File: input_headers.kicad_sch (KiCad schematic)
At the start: 13 parts, among them J1 171857-0003, J2 171856-0002, J6 171856-0002, J7 Conn_01x07, J8 USB_B_Micro, J9 TLW-104-05-T-D, U3 FT230XS-R

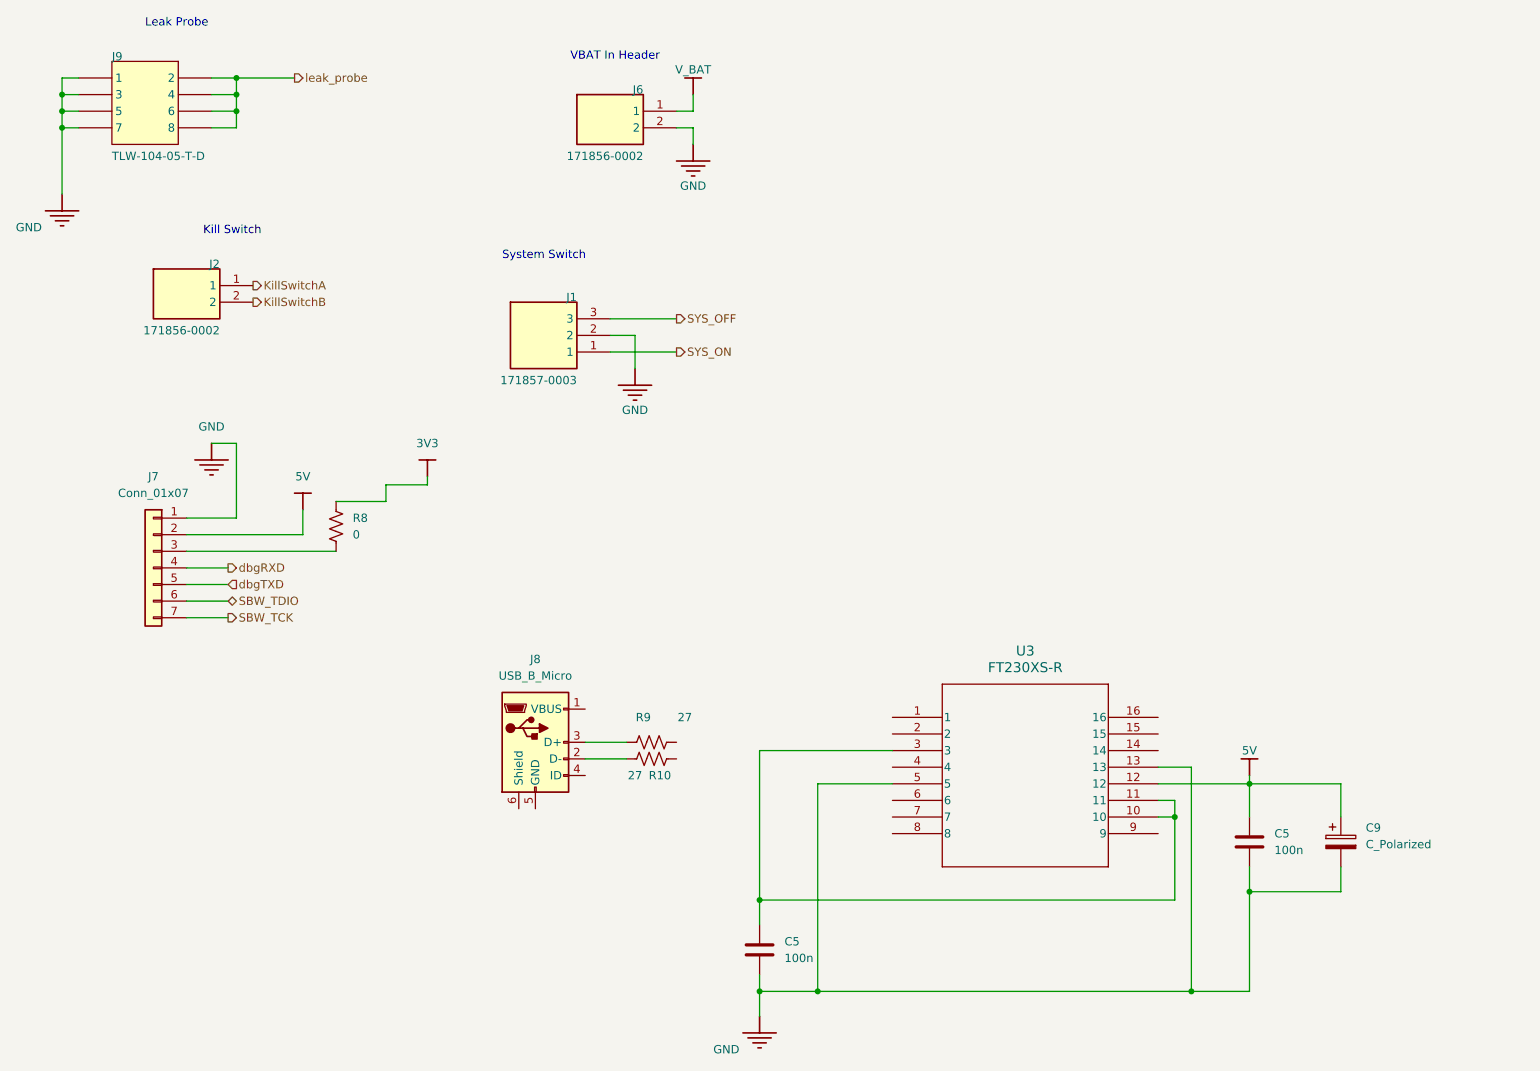
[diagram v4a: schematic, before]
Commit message: updated input headers schematic for FT232 chip
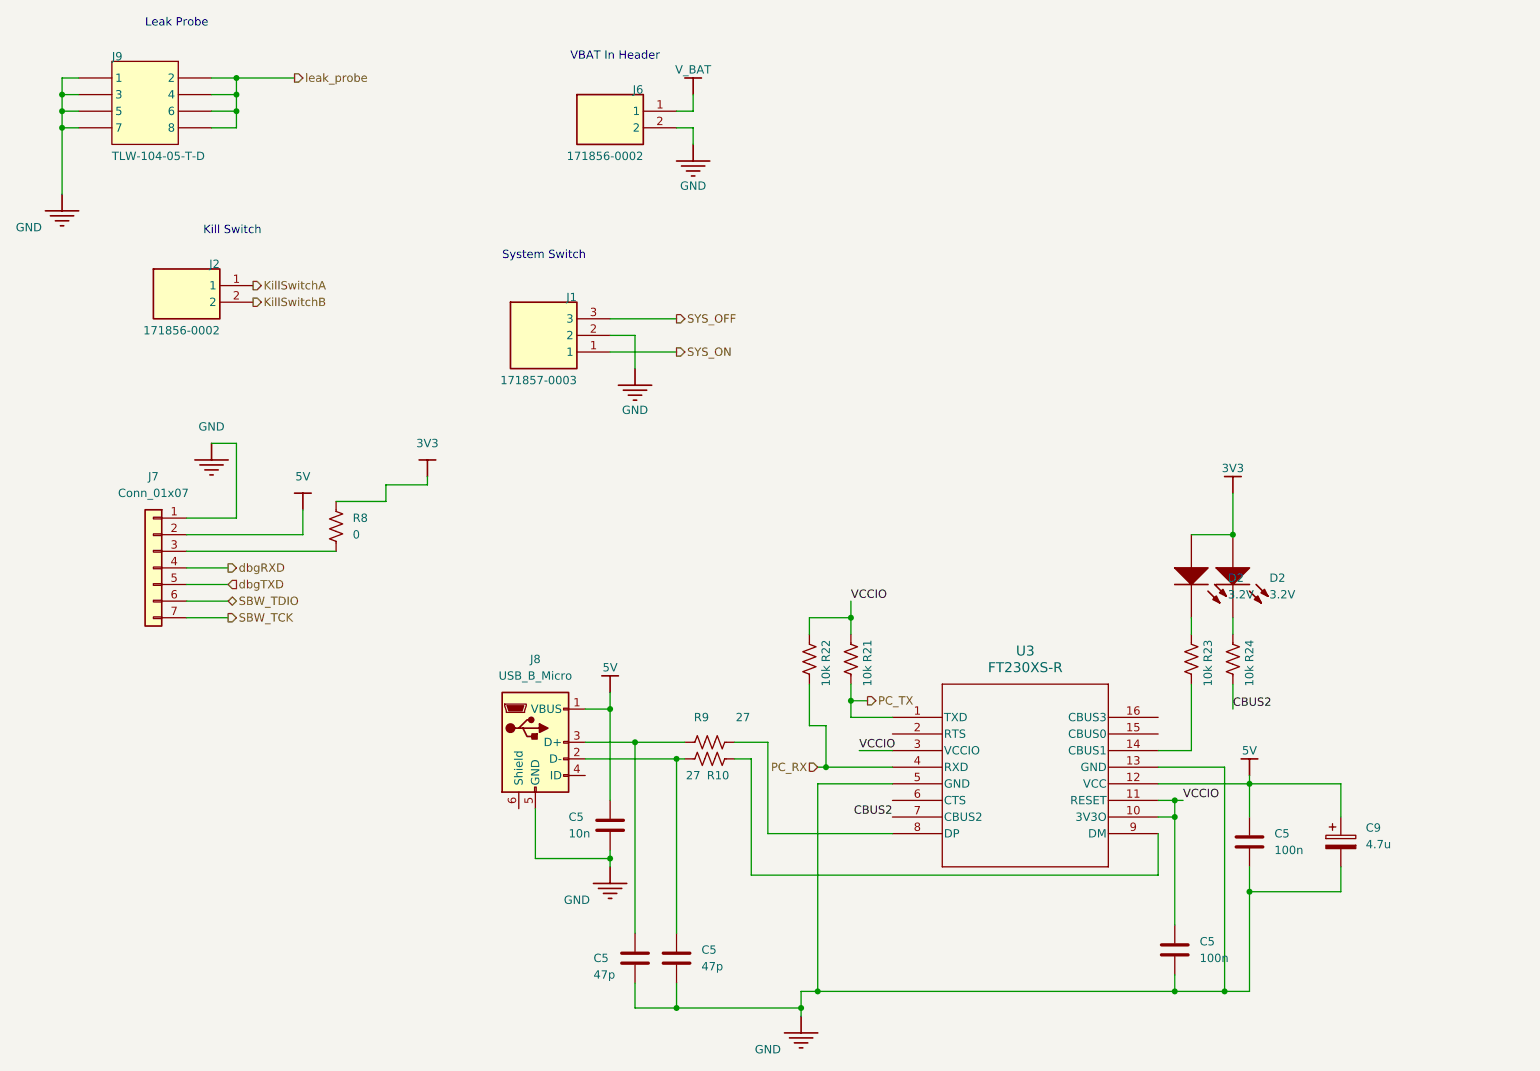
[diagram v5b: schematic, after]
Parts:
- removed C5: 100n, symbol Device:C
- added C5: 10n, symbol Device:C
- added C5 (x2): 47p, symbol Device:C
- added C5: 100n, symbol Device:C
- added D2 (x2): 3.2V, AltiumImport:0805_A, symbol MEB-altium-import:root_3_WE-LED_K1A2-2
- added R21, R22, R23, R24: 10k, symbol Device:R_US
- C9: value C_Polarized -> 4.7u
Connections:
- net 3V3: now also D2.2 (A), D2.2 (A)
- net 5V: now also J8.1 (VBUS), C5.1
- net GND: now also J8.5 (GND), C5.2, C5.2, C5.2, C5.2
- net PC_TX: now reaches U3.1 (TXD)
- net PC_TX: now also R21.1
- net VCCIO: now reaches U3.10 (3V3O), U3.11 (RESET), U3.3 (VCCIO)
- net VCCIO: now also C5.1, R21.2, R22.2
- net at U3.14 (CBUS1): now also R23.1
- net PC_RX: now reaches U3.4 (RXD)
- net PC_RX: now also R22.1
- net CBUS2: now reaches U3.7 (CBUS2)
- net CBUS2: now also R24.1
- net at U3.8 (DP): now also R9.2
- net at U3.9 (DM): now also R10.2
- net at J8.3 (D+), R9.1: now also C5.1
- net at J8.2 (D-), R10.1: now also C5.1
- new net: D2.1 (K), R23.2
- new net: D2.1 (K), R24.2
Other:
- moved on the sheet: R10, R9

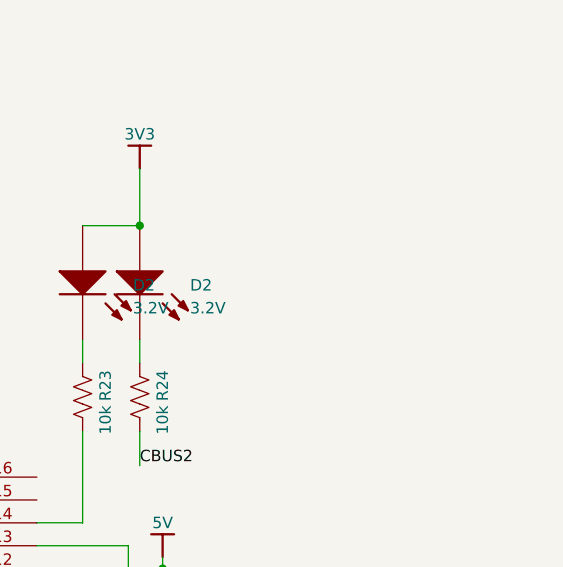
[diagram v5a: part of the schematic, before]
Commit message: Finalized schematic and began assigning footprints
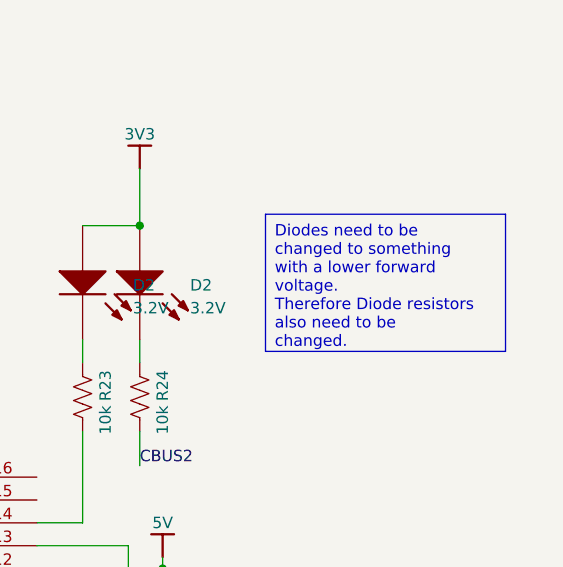
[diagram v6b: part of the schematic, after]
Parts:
- J8: footprint (none) -> Connector_USB:USB_Micro-B_GCT_USB3076-30-A
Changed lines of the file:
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@@
     (stroke (width 0) (type default))
+  )
+  (text_box "Diodes need to be changed to something with a lower forward voltage.\nTherefore Diode resistors also need to be changed.\n"
+    (at 204.47 96.52 0) (size 26.67 15.24)
+    (stroke (width 0) (type default))
+    (fill (type none))
+    (effects (font (size 1.27 1.27)) (justify left top))
   )
   (text "VBAT In Header" (at 102.87 25.4 0)
@@
       (effects (font (size 1.27 1.27)))
     )
-    (property "Footprint" "" (at 87.63 130.81 0)
-      (effects (font (size 1.27 1.27)) hide)
-    )
+    (property "Footprint" "Connector_USB:USB_Micro-B_GCT_USB3076-30-A" (at 87.63 130.81 0)
+      (effects (font (size 1.27 1.27)) hide)
+    )

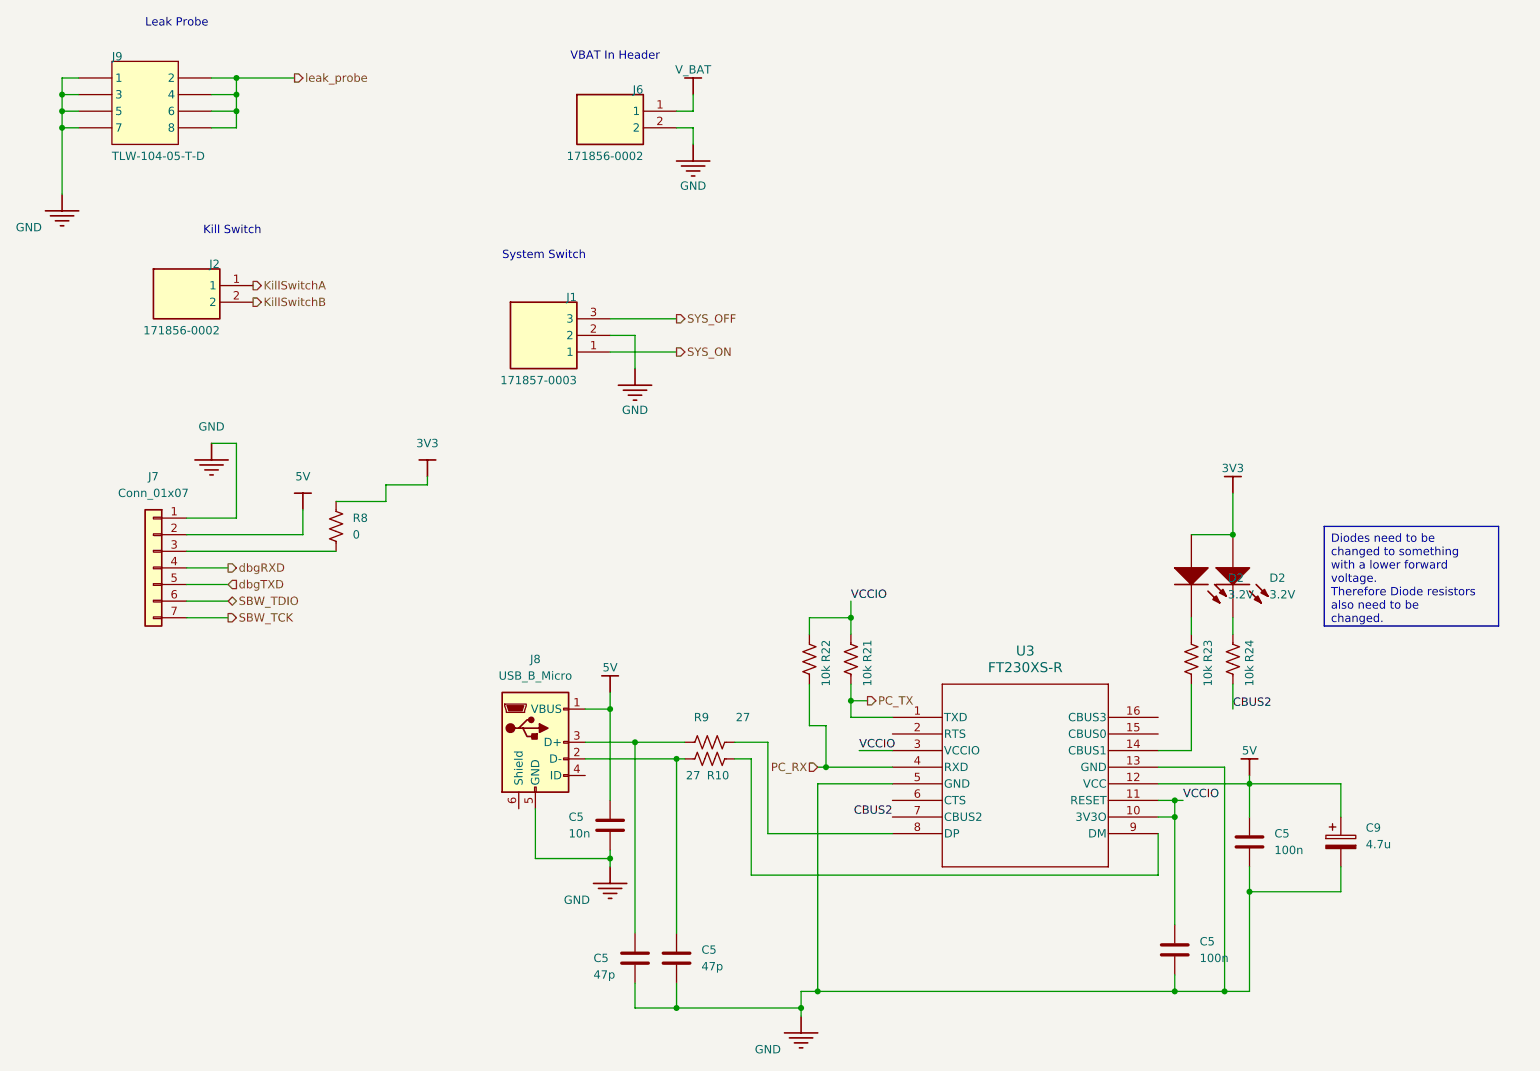
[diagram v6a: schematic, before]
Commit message: updated power and ground symbols in schematic to kicad library version
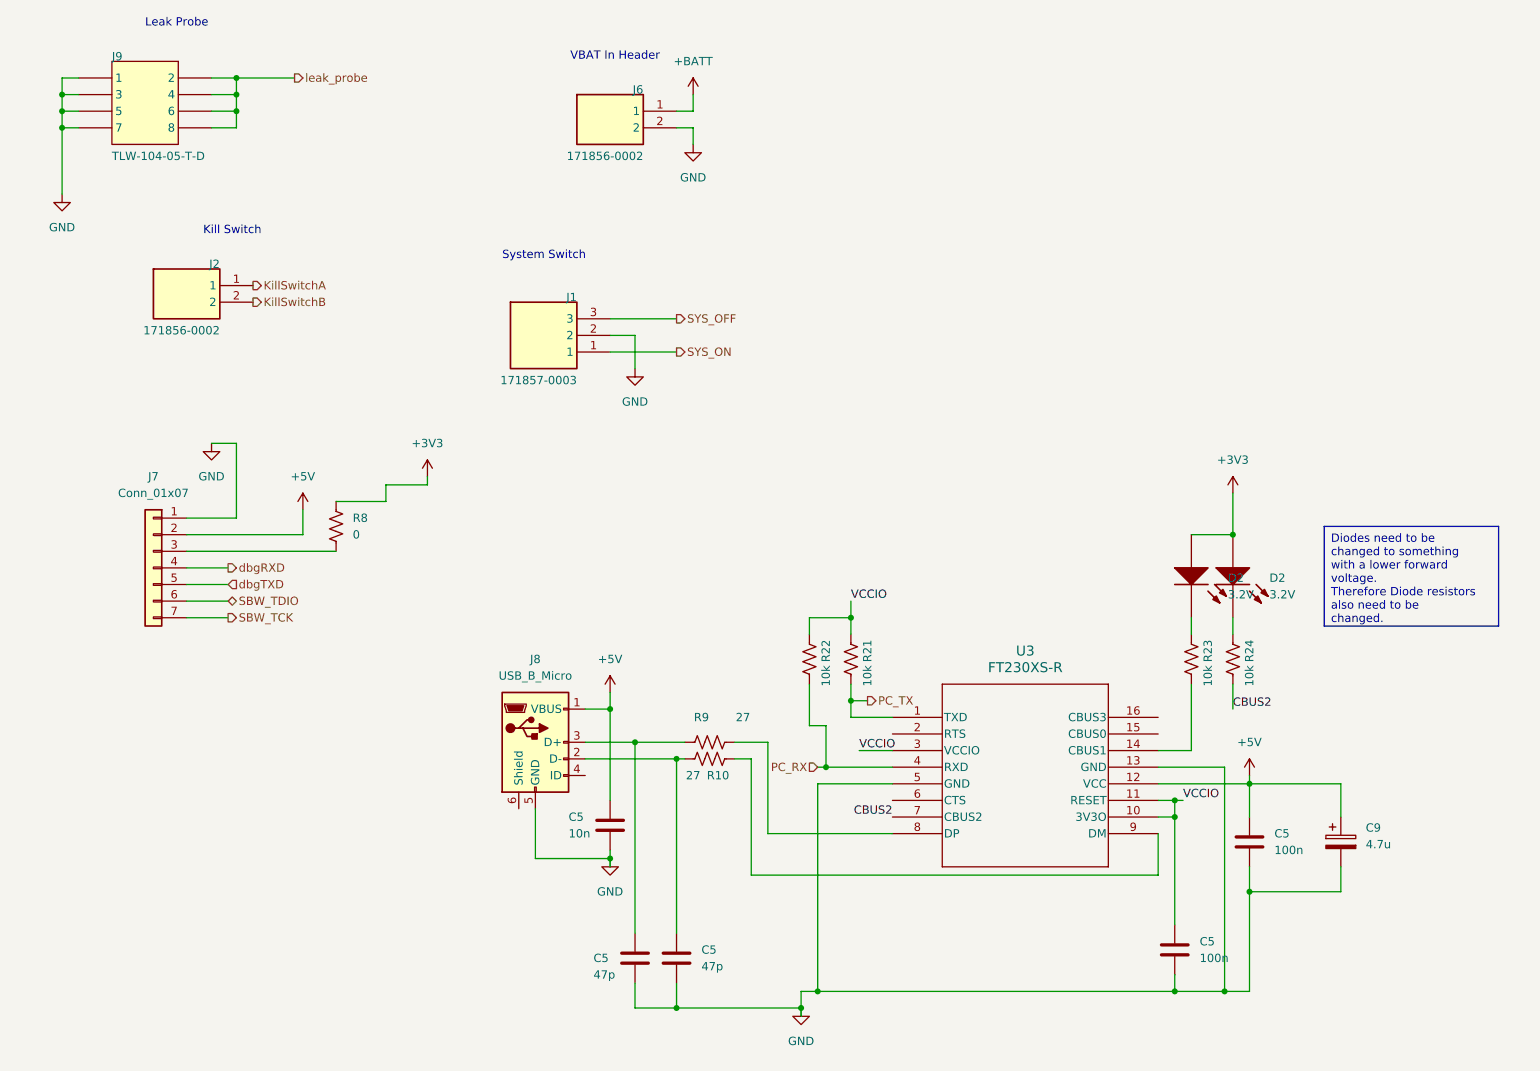
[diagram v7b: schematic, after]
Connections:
- net 3V3 renamed +3V3
- net 5V renamed +5V
- net V_BAT renamed +BATT
